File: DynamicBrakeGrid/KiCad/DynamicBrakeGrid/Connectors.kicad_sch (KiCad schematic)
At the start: 46 parts, among them J1 1987724, J10 5442251, J11 5442251, J12 5442251, J13 38969-0002, J16 1548129, J17 1548129, J2 1987724, J22 1548129, J23 1548129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

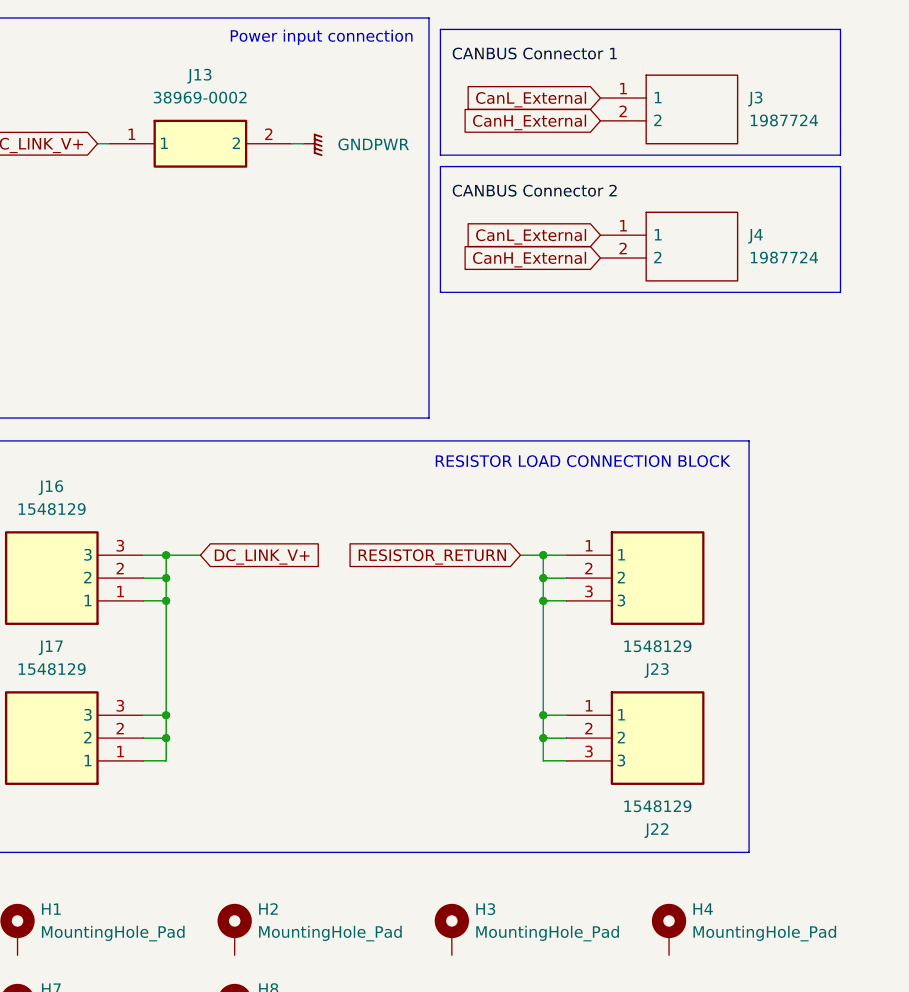
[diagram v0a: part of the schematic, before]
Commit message: Update Schematics, Inverter, Gate Driver, Mechanical, Software
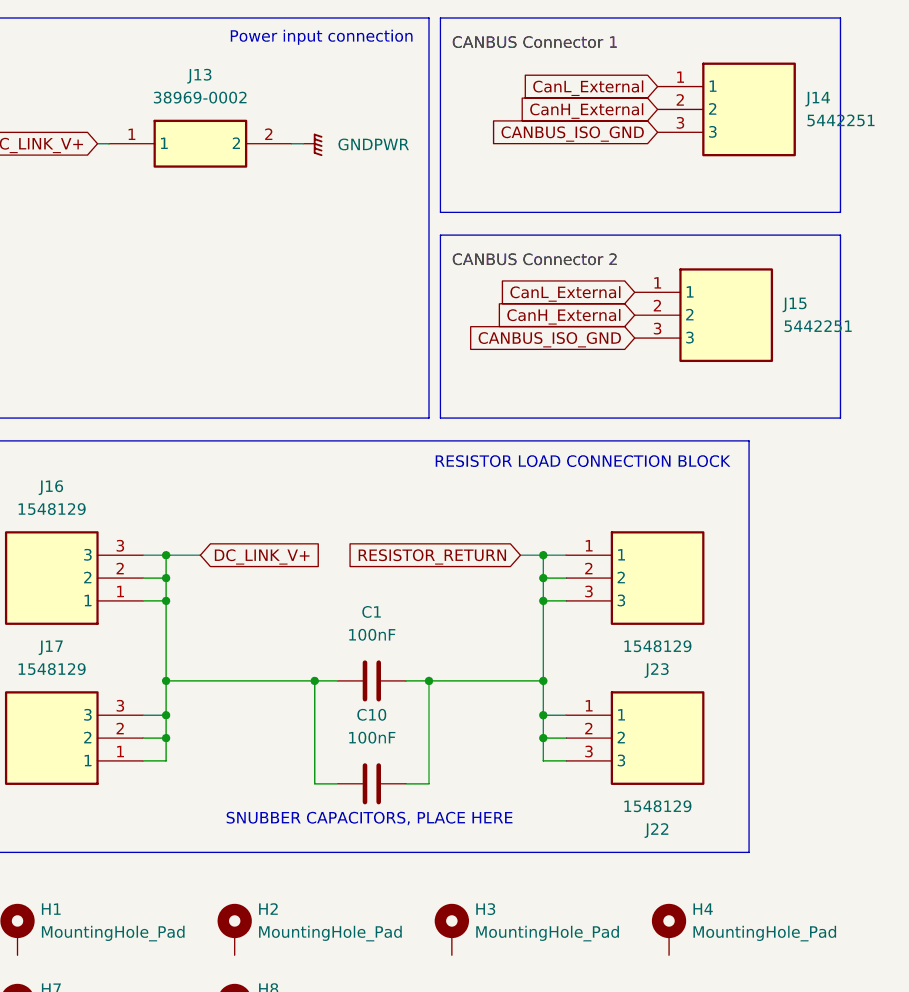
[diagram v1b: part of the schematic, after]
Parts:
- removed J3, J4: 1987724, InverterCom:1987724, symbol InverterCom:1987724
- added C1, C10: 100nF, symbol Device:C
- added J14, J15: 5442251, InverterCom:5442251, symbol InverterCom:5442251
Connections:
- net CanH_External: now also J14.2, J15.2
- net CanL_External: now also J14.1, J15.1
- net DC_LINK_V+: now also C1.1, C10.1
- net RESISTOR_RETURN: now also C1.2, C10.2
- new net CANBUS_ISO_GND: J14.3, J15.3
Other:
- note added: "SNUBBER CAPACITORS, PLACE HERE"
